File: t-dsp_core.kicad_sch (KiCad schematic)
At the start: 273 parts, among them IC1 Logic Level Shifter - 74HCT2G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, J1 jumper, J10 JST-XH Connector, J11 JST-XH Connector, J12 RGB LED HEADEER, J13 Conn_01x02, J14 Conn_01x03, J15 Conn_01x01, J16 Conn_01x02, J17 Conn_02x04_Odd_Even, J18 Conn_02x02_Odd_Even, J19 Conn_01x01, J2 GROUND HEADER, J20 Conn_01x01, J21 jumper, J22 35RAPC4BV4, J23 35RAPC4BV4, J24 Conn_01x04, J25 PRT-14417, J26 73725-0110BLF, J27 GROUND HEADER, J3 jumper, J3V108 jumper, J4 jumper, J5 jumper, J6 jumper, J7 jumper, J8 PJRAS2X1S01X, J9 PJRAS2X1S01X, Q1 DMG2307L-7, Q2 DMG2307L-7, SW1 SW_SPST, SW10 SW_SPST, SW2 TL1105WF160Q - 3.15mm actuator, SW3 SW_SPST, SW4 SW_SPST, SW5 RotaryEncoder_Switch_MP, SW6 TL1105WF160Q - 3.15mm actuator, SW7 TL1105WF160Q - 3.15mm actuator, SW8 TL1105WF160Q - 3.15mm actuator, SW9 SW_SPST, T108 Tab, T109 Tab, T110 Tab, T111 Tab, U1 Teensy 4.1 - DEVKIT, U10 TPD4E02B04DQA, U109 3.3v LDO - LP5907-3.3, U11 Dual Buffer - SN74LVC2G125DCTR, U13 ESP32-S3-WROOM-1, U15 LT3045EMSE#TRPBF, U2 ESP32-DevKitC - DEVKIT, U3 Power Mux & Protect - TPS2116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, U4 Optoisolators - H11L1SM - 6-S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, U5 Dual Buffer - SN74LVC2G125DCTR, U6 Dual Buffer - SN74LVC2G125DCTR, U7 Dual Buffer - SN74LVC2G125DCTR, U8 Dual Buffer - SN74LVC2G125DCTR, U9 Dual Buffer - 74HCT2G17GW,125, Y1 audio clock

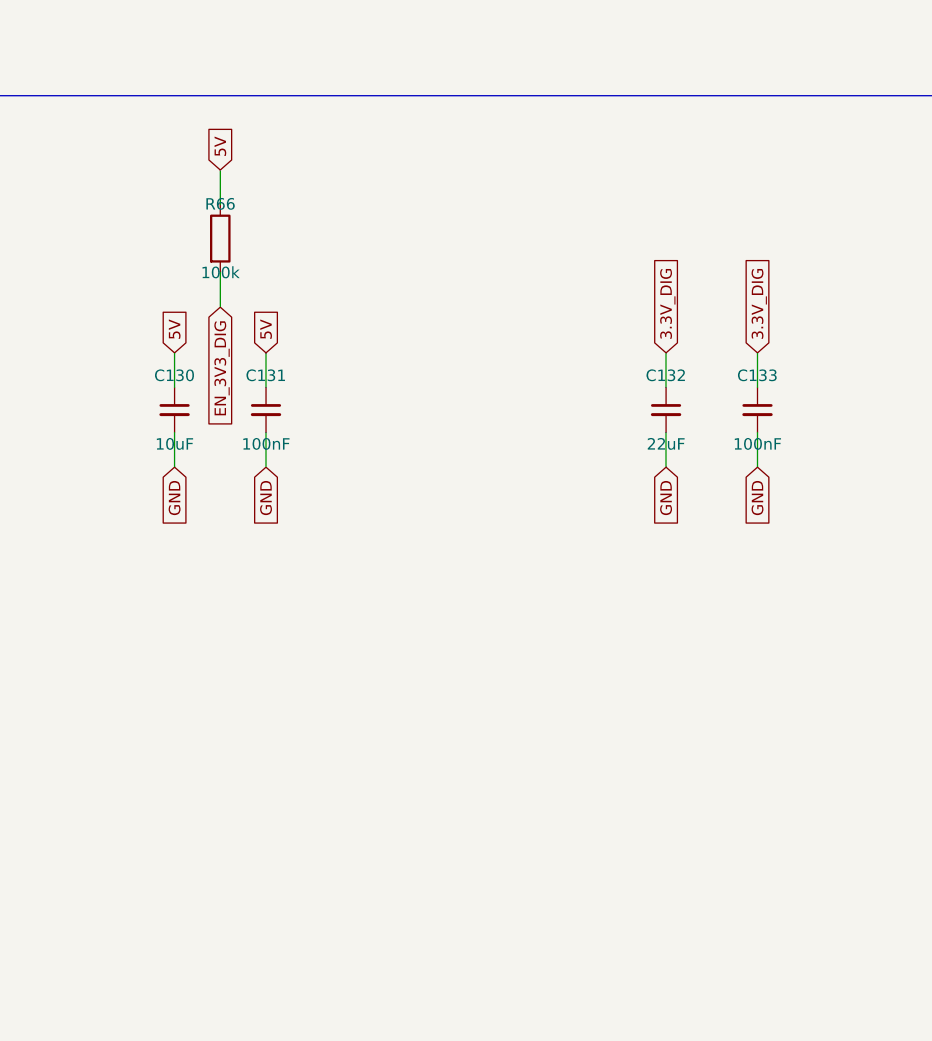
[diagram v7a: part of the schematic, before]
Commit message: Wire U12 (TLV76733DRVR) - the 3.3V_DIG rail now has a source
Completes the digital supply block for the ESP32-S3. U12 was placed in
eeschema; Konnect cannot place symbols that are not already embedded in
the schematic's lib_symbols, so that step had to be manual.

  pin 6 IN   -> 5V
  pin 1 OUT  -> 3.3V_DIG
  pin 2 SNS  -> 3.3V_DIG   (remote sense, required on the fixed version)
  pin 4 EN   -> EN_3V3_DIG (100k pull-up to 5V via R66)
  pins 3/5/7 -> GND        (GND, GND, thermal PAD)

Footprint set to Package_SON:WSON-6-1EP_2x2mm_P0.65mm_EP1x1.6mm_ThermalVias.
create_symbol had silently dropped the footprint and datasheet arguments
when the library was generated, leaving both empty; set here on the
instance instead.

Netlist confirms 3.3V_DIG is now driven:
  U12.1 power_out, U12.2 input, U13.2 power_in, C132.1, C133.1

connect_to_net stripped the User paper dimensions again; restored in the
same pass.

Still outstanding: six duplicate reference designators (C43, C44, R55,
R56, R57, R61) need Annotate in eeschema - Konnect's rename writes only
the Reference property and leaves the instances block, which is what
KiCad netlists from.

Co-Authored-By: Claude Opus 5 <noreply@anthropic.com>
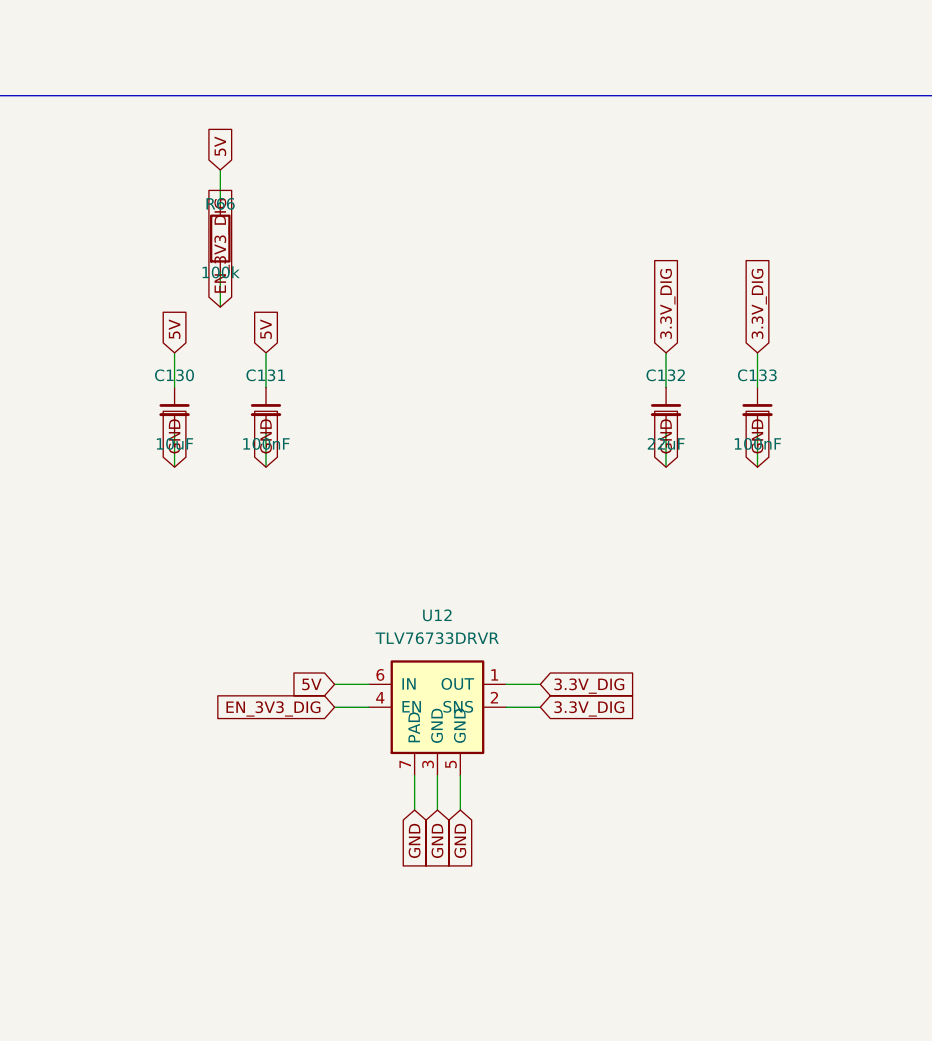
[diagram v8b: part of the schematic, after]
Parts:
- added U12: TLV76733DRVR, Package_SON:WSON-6-1EP_2x2mm_P0.65mm_EP1x1.6mm_ThermalVias, symbol TLV76733DRVR:TLV76733DRVR
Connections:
- net 3.3V_DIG: now also U12.1 (OUT), U12.2 (SNS)
- net 5V: now also U12.6 (IN)
- net EN_3V3_DIG: now also U12.4 (EN)
- net GND: now also U12.3 (GND), U12.5 (GND), U12.7 (PAD)
